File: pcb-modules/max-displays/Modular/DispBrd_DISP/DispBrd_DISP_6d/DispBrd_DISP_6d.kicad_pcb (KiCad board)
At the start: 2 copper layers, 43.7 x 19.3 mm, 4 parts, among them P7 Disp6

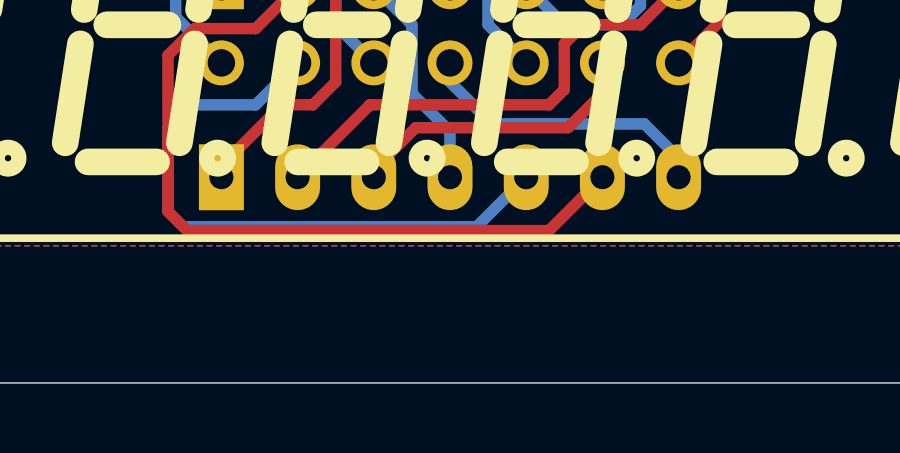
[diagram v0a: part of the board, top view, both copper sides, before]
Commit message: Max Display panels, modular version FIX: Rear connector rotated 180deg on boards [3+2d], [3+3d], [6x1d] All boards: Silkscreen text on rear oriented correctly; board name added; Format update to KiCAD 6.0.6
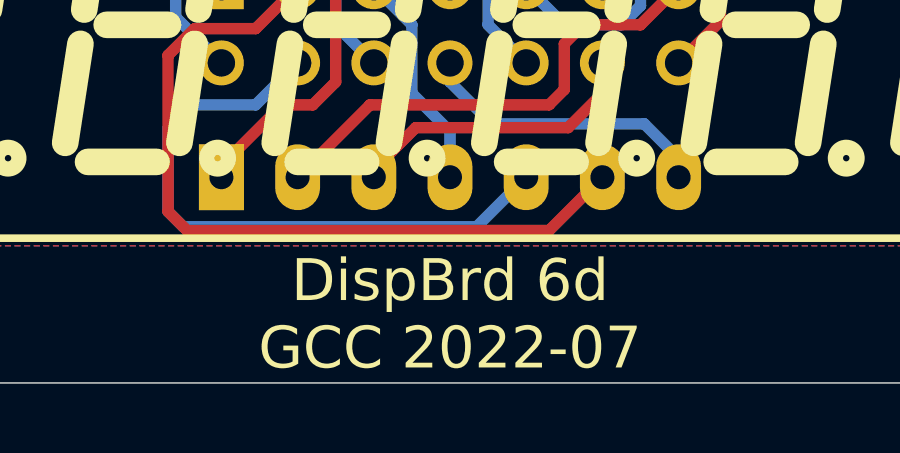
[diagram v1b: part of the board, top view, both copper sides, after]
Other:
- board text added: "DispBrd 6d GCC 2022-07"
- board text added: "K5 K3 K1 G E C A"
- board text added: "K6 K4 K2 dp F D B"
- board text removed: "A C E G K1 K3 K5"
- board text removed: "B D F dp K2 K4 K6"
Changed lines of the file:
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@@
   )
   (gr_rect (start 35.56 25.4) (end 79.248 44.704) (layer "Edge.Cuts") (width 0.05) (fill none))
-  (gr_text "B  D  F dp K2 K4 K6" (at 57.658 35.814 180) (layer "B.SilkS")
+  (gr_text "K6 K4 K2 dp F  D  B" (at 57.658 35.814) (layer "B.SilkS")
     (effects (font (size 1.27 1.016) (thickness 0.2032)) (justify mirror))
   )
-  (gr_text "A  C  E  G K1 K3 K5" (at 57.658 29.718 180) (layer "B.SilkS")
+  (gr_text "K5 K3 K1 G  E  C  A" (at 57.658 29.718) (layer "B.SilkS")
     (effects (font (size 1.27 1.016) (thickness 0.2032)) (justify mirror))
   )
+  (gr_text "DispBrd 6d\nGCC 2022-07" (at 57.404 42.418) (layer "B.SilkS")
+    (effects (font (size 1.397 1.397) (thickness 0.254)) (justify mirror))
+  )
+  (gr_text "DispBrd 6d\nGCC 2022-07" (at 57.404 42.418) (layer "F.SilkS")
+    (effects (font (size 1.397 1.397) (thickness 0.254)))
+  )
   (segment (start 49.784 30.226) (end 52.324 27.686) (width 0.381) (layer "F.Cu") (net 1))
